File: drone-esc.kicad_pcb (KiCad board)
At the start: 6 copper layers, 34 x 34 mm, 194 parts, among them J1 SM08B-SRSS-TB_LF__SN_, Q1 IRLHS6242, Q10 IRLHS6242, Q11 IRLHS6242, Q12 IRLHS6242, Q13 IRLHS6242, Q14 IRLHS6242, Q15 IRLHS6242, Q16 IRLHS6242, Q17 IRLHS6242, Q18 IRLHS6242, Q19 IRLHS6242, Q2 IRLHS6242, Q20 IRLHS6242, Q21 IRLHS6242, Q22 IRLHS6242, Q23 IRLHS6242, Q24 IRLHS6242, Q3 IRLHS6242, Q4 IRLHS6242, Q5 IRLHS6242, Q6 IRLHS6242, Q7 IRLHS6242, Q8 IRLHS6242, Q9 IRLHS6242, U10 DGD05473FNQ-7, U11 DGD05473FNQ-7, U12 AT32F421G8U7, U13 DGD05473FNQ-7, U14 DGD05473FNQ-7, U15 DGD05473FNQ-7, U16 AT32F421G8U7, U17 DGD05473FNQ-7, U18 DGD05473FNQ-7, U19 DGD05473FNQ-7, U2 INA186A3IDCKR, U20 AT32F421G8U7, U3 TLV76733DRVR, U4 TPS61023DRLR, U5 AT32F421G8U7, U6 DGD05473FNQ-7, U7 DGD05473FNQ-7, U8 DGD05473FNQ-7, U9 DGD05473FNQ-7

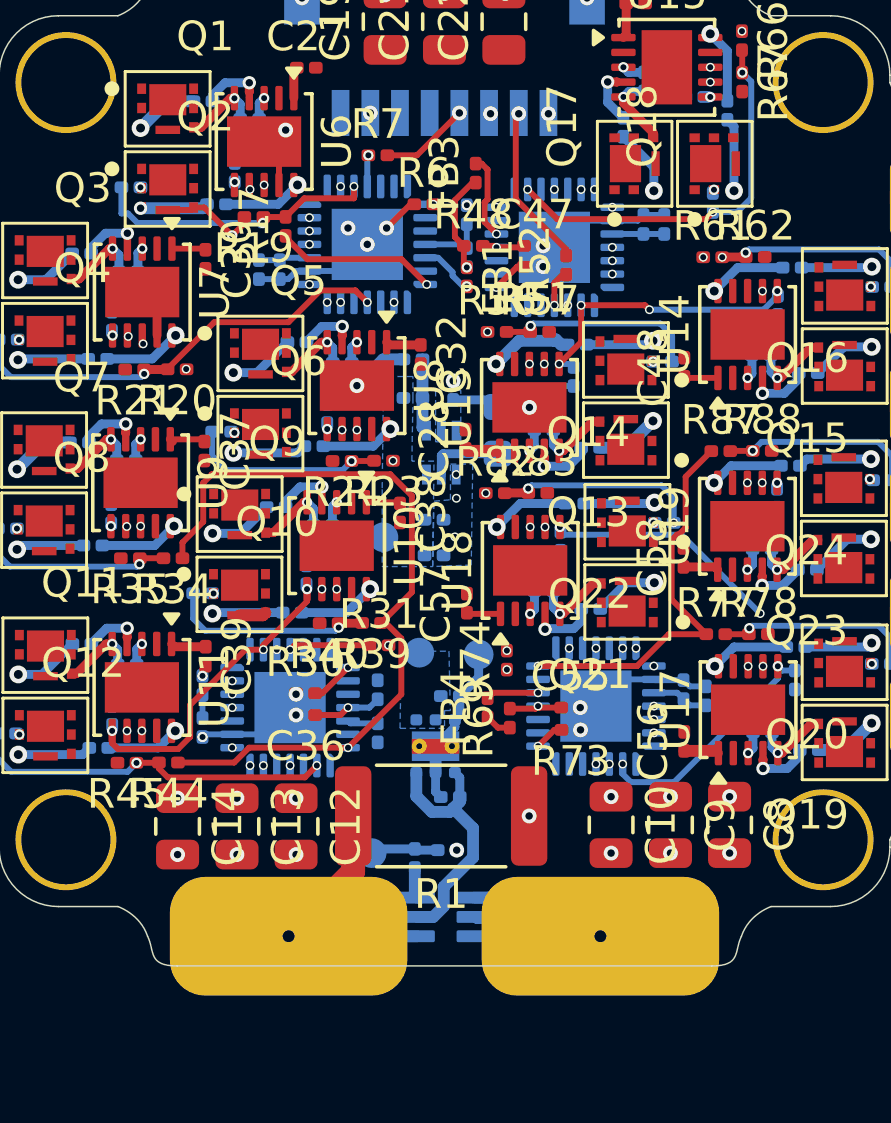
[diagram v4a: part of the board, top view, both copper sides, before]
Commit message: +3.3V power plane
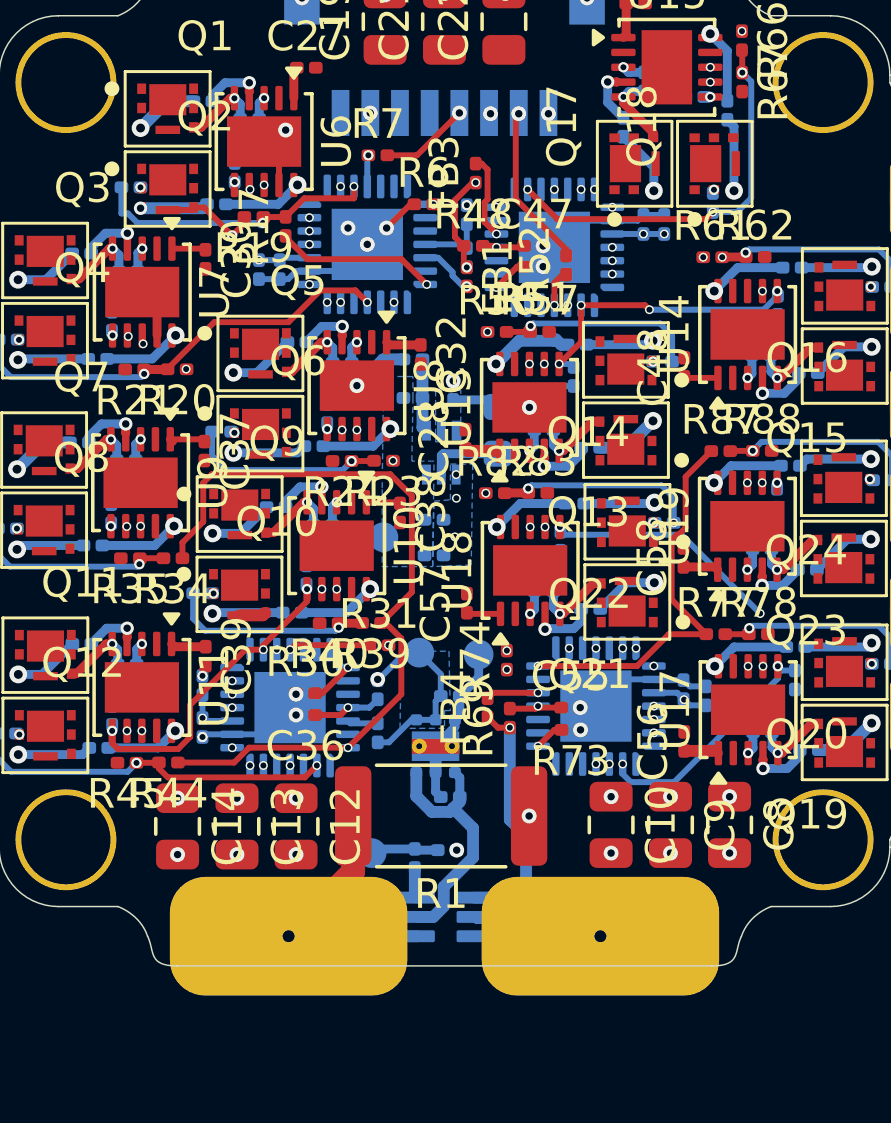
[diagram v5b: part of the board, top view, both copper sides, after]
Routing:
- net +3.3V: track 11.7 -> 42.2 mm, vias 1 -> 9
- net GND: track 40.4 -> 37.1 mm
- added copper zone on In3.Cu, net +3.3V

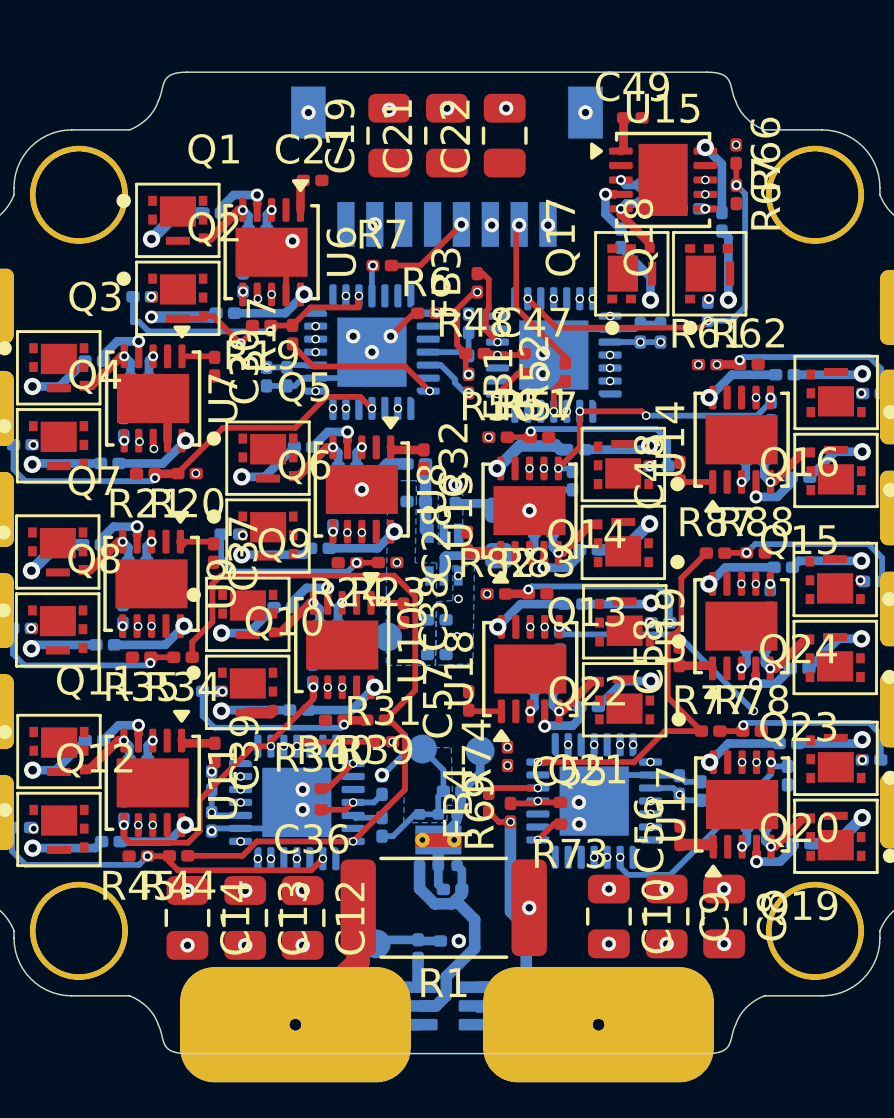
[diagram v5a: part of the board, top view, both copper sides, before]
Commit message: routed +5V
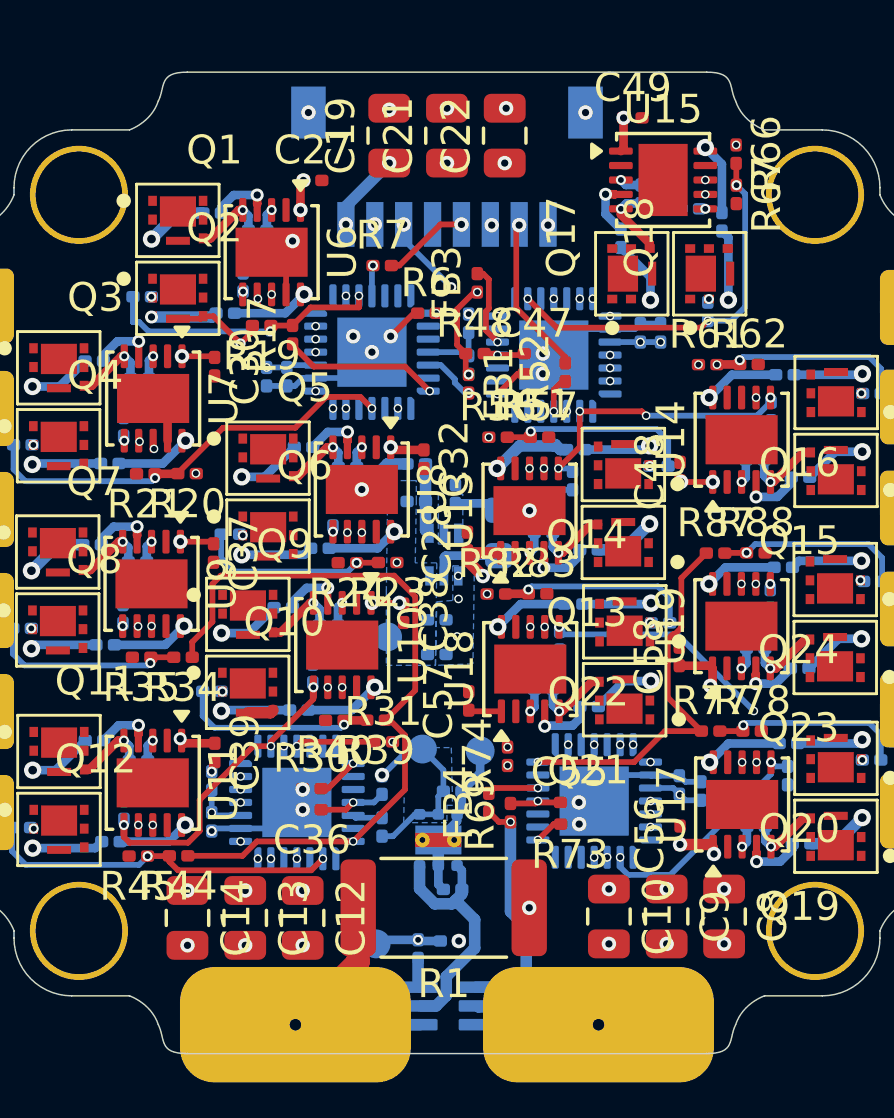
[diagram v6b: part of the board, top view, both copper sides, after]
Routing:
- net /CURR: track 2.30 -> 28.2 mm, vias 0 -> 3
- net +BATT: track 10.3 -> 13.0 mm, vias 7 -> 11
- net +5V: track 14.2 -> 16.2 mm, vias 0 -> 15
- net +3.3V: track 42.2 -> 43.2 mm
- net GND: vias 33 -> 32
- added copper zone on In3.Cu, net +5V

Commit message: lastest
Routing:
- net GND: track 37.1 -> 64.0 mm
- net +BATT: track 13.0 -> 21.1 mm, vias 11 -> 12
- net /ESC3/MotorC: track 2.68 -> 8.31 mm, vias 2 -> 6
- added copper zone on F.Cu, net /ESC3/MotorC
